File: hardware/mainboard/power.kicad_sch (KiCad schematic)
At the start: 19 parts, among them J1 Eurorack Power, U1 LD1117-3.3, U2 LM4040DBZ-10

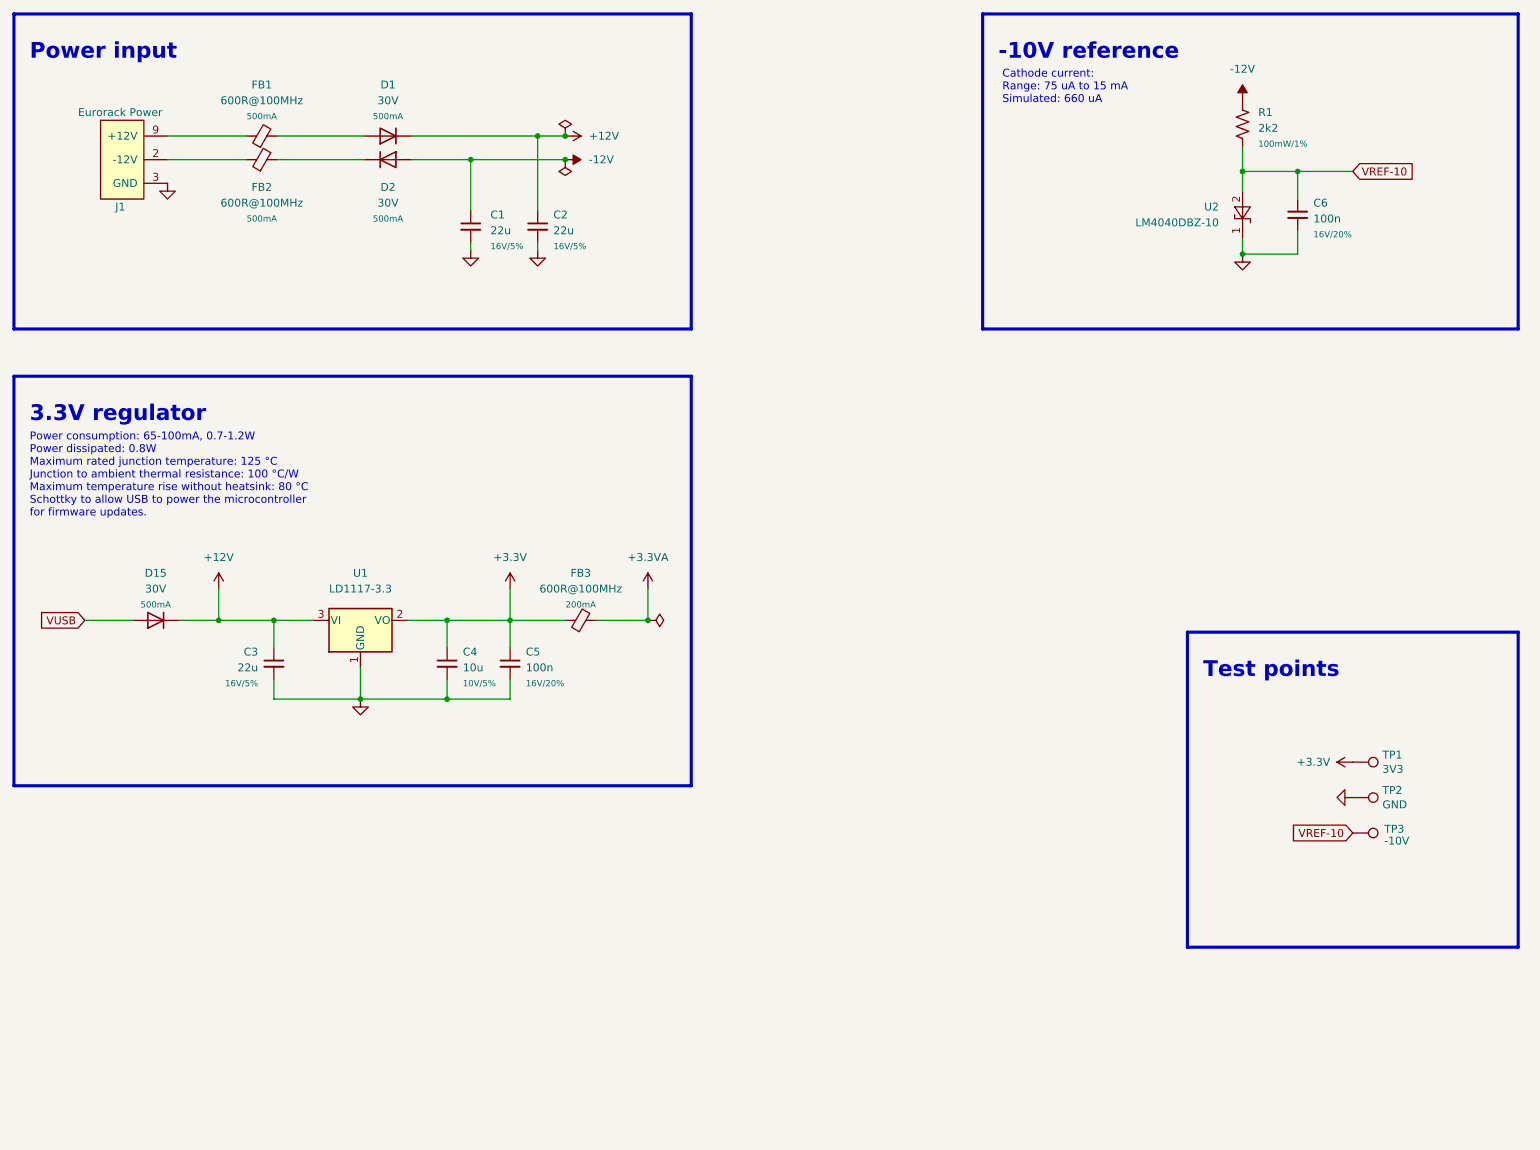
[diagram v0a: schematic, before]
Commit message: hardware: minor tweaks to power schematic's layout
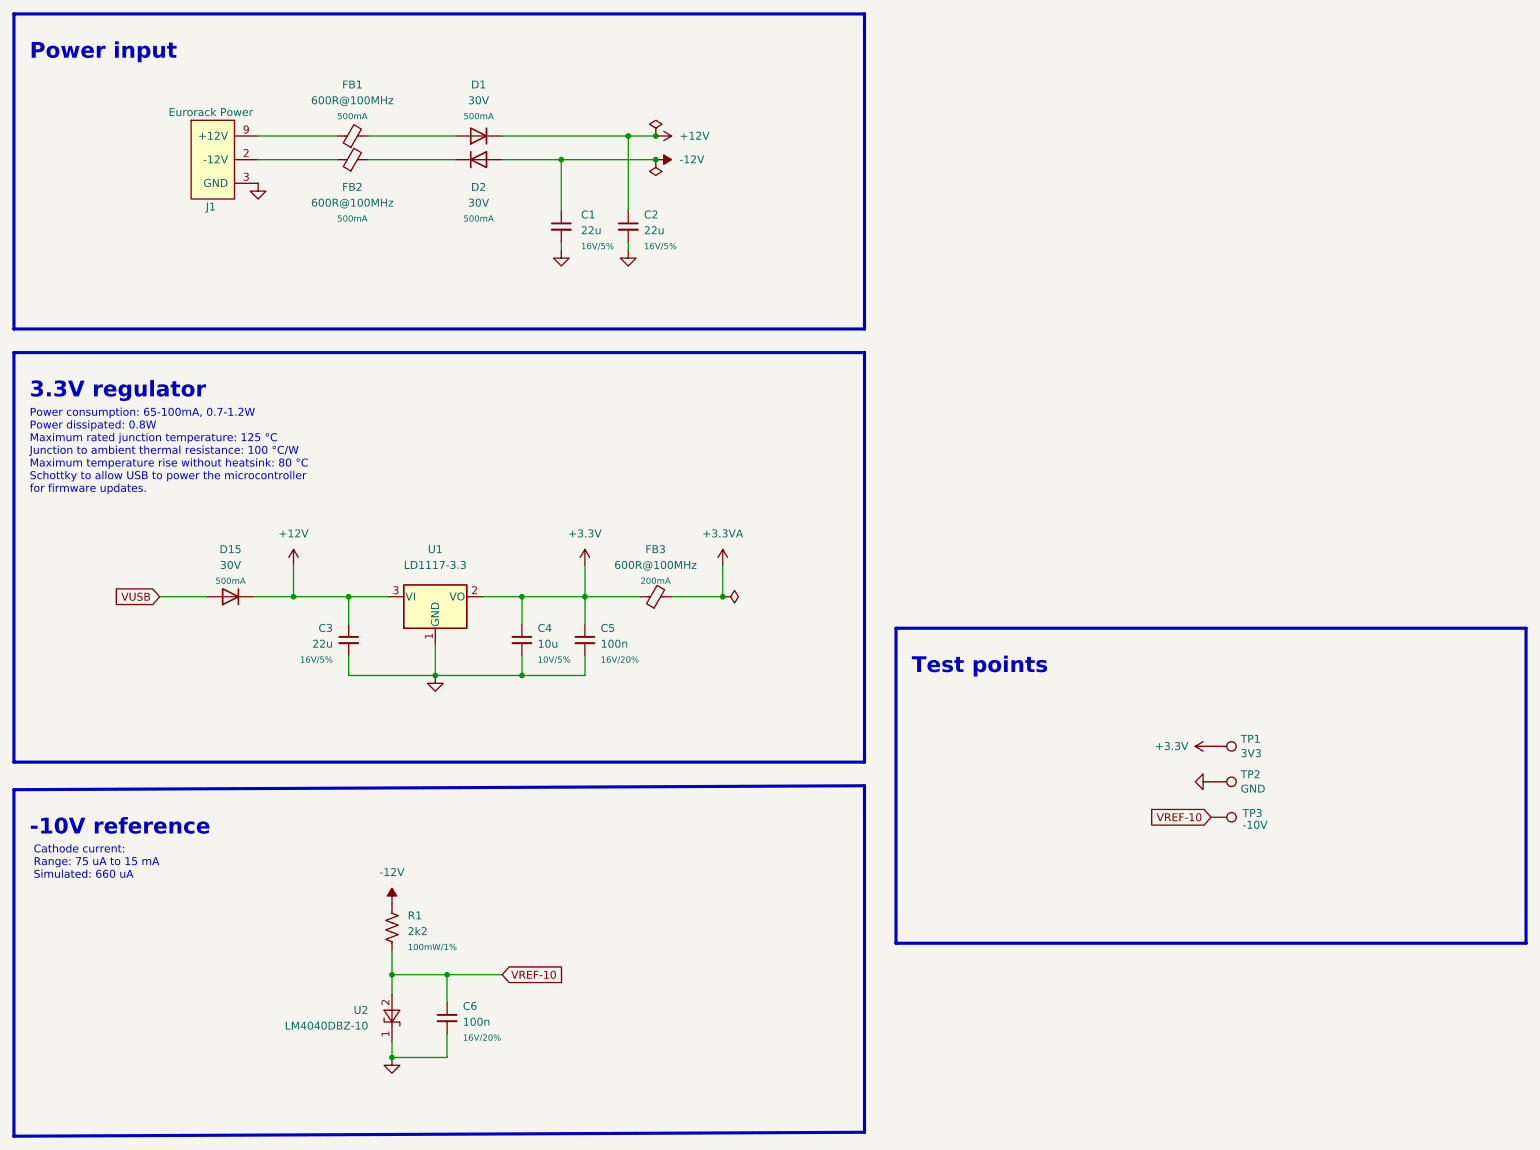
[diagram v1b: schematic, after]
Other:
- moved on the sheet: C1, C2, C3, C4, C5, C6, D1, D15, D2, FB1, FB2, FB3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

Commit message: hardware: use winterbloom footprints for C, R, and L
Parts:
- C1, C2, C3: footprint Capacitor_SMD:C_0805_2012Metric_Pad1.18x1.45mm_HandSolder -> winterbloom:C_0805_HandSolder
- C4: footprint Capacitor_SMD:C_0603_1608Metric_Pad1.08x0.95mm_HandSolder -> winterbloom:C_0603_HandSolder
- C5, C6: footprint Capacitor_SMD:C_0402_1005Metric_Pad0.74x0.62mm_HandSolder -> winterbloom:C_0402_HandSolder
- FB1, FB2, FB3: footprint Inductor_SMD:L_0603_1608Metric_Pad1.05x0.95mm_HandSolder -> winterbloom:L_0603_HandSolder
- R1: footprint Resistor_SMD:R_0402_1005Metric_Pad0.72x0.64mm_HandSolder -> winterbloom:R_0402_HandSolder
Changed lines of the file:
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@@
       (effects (font (size 1.27 1.27)) (justify right))
     )
-    (property "Footprint" "Capacitor_SMD:C_0805_2012Metric_Pad1.18x1.45mm_HandSolder" (id 2) (at 71.755 118.745 0)
+    (property "Footprint" "winterbloom:C_0805_HandSolder" (id 2) (at 71.755 118.745 0)
       (effects (font (size 1.27 1.27)) hide)
     )
@@
       (effects (font (size 1.27 1.27)) (justify left))
     )
-    (property "Footprint" "Capacitor_SMD:C_0603_1608Metric_Pad1.08x0.95mm_HandSolder" (id 2) (at 99.695 118.745 0)
+    (property "Footprint" "winterbloom:C_0603_HandSolder" (id 2) (at 99.695 118.745 0)
       (effects (font (size 1.27 1.27)) hide)
     )
@@
       (effects (font (size 1.27 1.27)) (justify left))
     )
-    (property "Footprint" "Capacitor_SMD:C_0402_1005Metric_Pad0.74x0.62mm_HandSolder" (id 2) (at 110.8202 122.555 0)
+    (property "Footprint" "winterbloom:C_0402_HandSolder" (id 2) (at 110.8202 122.555 0)
       (effects (font (size 1.27 1.27)) hide)
     )
@@
     (property "Reference" "FB3" (id 0) (at 121.2469 104.14 90))
     (property "Value" "600R@100MHz" (id 1) (at 121.2469 106.68 90))
-    (property "Footprint" "Inductor_SMD:L_0603_1608Metric_Pad1.05x0.95mm_HandSolder" (id 2) (at 121.285 113.538 90)
+    (property "Footprint" "winterbloom:L_0603_HandSolder" (id 2) (at 121.285 113.538 90)
       (effects (font (size 1.27 1.27)) hide)
     )
@@
     (property "Reference" "FB2" (id 0) (at 72.3519 45.72 90))
     (property "Value" "600R@100MHz" (id 1) (at 72.3519 48.26 90))
-    (property "Footprint" "Inductor_SMD:L_0603_1608Metric_Pad1.05x0.95mm_HandSolder" (id 2) (at 72.39 43.053 90)
+    (property "Footprint" "winterbloom:L_0603_HandSolder" (id 2) (at 72.39 43.053 90)
       (effects (font (size 1.27 1.27)) hide)
     )
@@
     (property "Reference" "FB1" (id 0) (at 72.3519 29.21 90))
     (property "Value" "600R@100MHz" (id 1) (at 72.3519 31.75 90))
-    (property "Footprint" "Inductor_SMD:L_0603_1608Metric_Pad1.05x0.95mm_HandSolder" (id 2) (at 72.39 39.243 90)
+    (property "Footprint" "winterbloom:L_0603_HandSolder" (id 2) (at 72.39 39.243 90)
       (effects (font (size 1.27 1.27)) hide)
     )
@@
       (effects (font (size 1.27 1.27)) (justify left))
     )
-    (property "Footprint" "Resistor_SMD:R_0402_1005Metric_Pad0.72x0.64mm_HandSolder" (id 2) (at 79.756 165.354 90)
+    (property "Footprint" "winterbloom:R_0402_HandSolder" (id 2) (at 79.756 165.354 90)
       (effects (font (size 1.27 1.27)) hide)
     )
@@
       (effects (font (size 1.27 1.27)) (justify left))
     )
-    (property "Footprint" "Capacitor_SMD:C_0402_1005Metric_Pad0.74x0.62mm_HandSolder" (id 2) (at 88.5952 183.515 0)
+    (property "Footprint" "winterbloom:C_0402_HandSolder" (id 2) (at 88.5952 183.515 0)
       (effects (font (size 1.27 1.27)) hide)
     )
@@
       (effects (font (size 1.27 1.27)) (justify left))
     )
-    (property "Footprint" "Capacitor_SMD:C_0805_2012Metric_Pad1.18x1.45mm_HandSolder" (id 2) (at 107.0102 55.88 0)
+    (property "Footprint" "winterbloom:C_0805_HandSolder" (id 2) (at 107.0102 55.88 0)
       (effects (font (size 1.27 1.27)) hide)
     )
@@
       (effects (font (size 1.27 1.27)) (justify left))
     )
-    (property "Footprint" "Capacitor_SMD:C_0805_2012Metric_Pad1.18x1.45mm_HandSolder" (id 2) (at 117.8052 55.88 0)
-      (effects (font (size 1.27 1.27)) hide)
-    )
+    (property "Footprint" "winterbloom:C_0805_HandSolder" (id 2) (at 117.8052 55.88 0)
+      (effects (font (size 1.27 1.27)) hide)
+    )

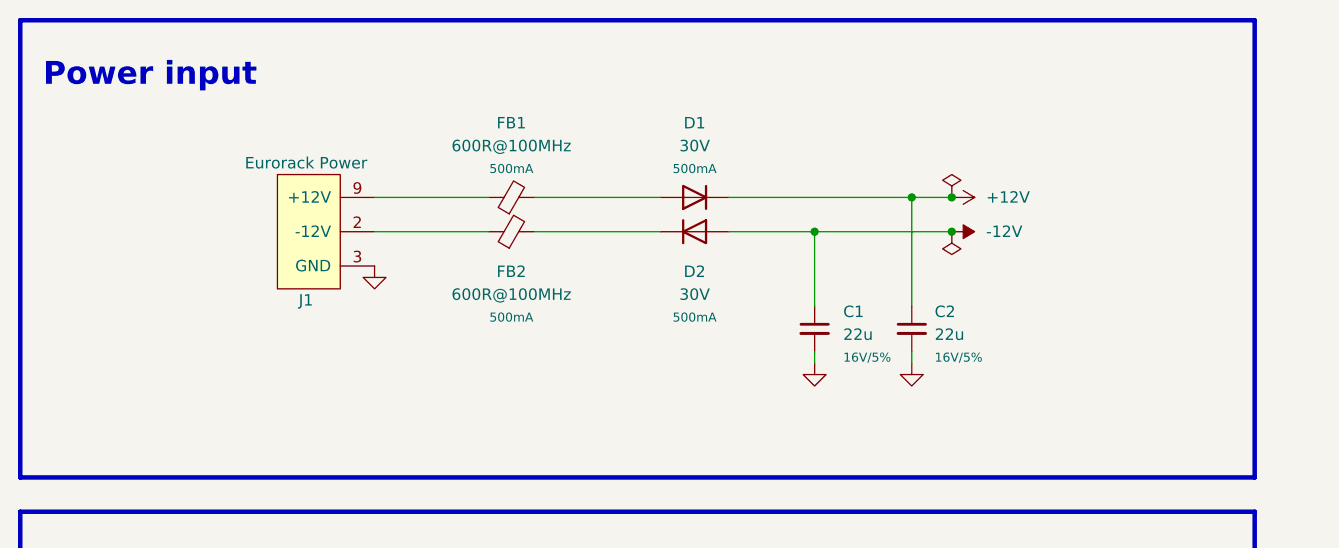
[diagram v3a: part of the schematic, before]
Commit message: hardware: spruce up some labels
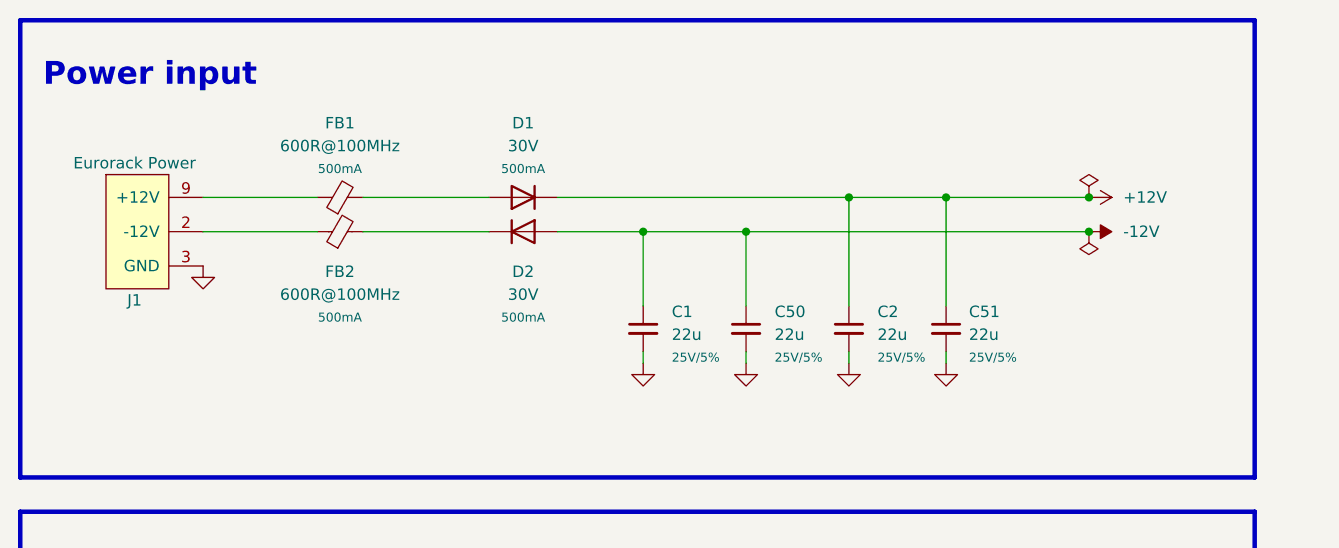
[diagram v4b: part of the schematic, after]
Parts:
- added C50, C51: 22u, winterbloom:C_0805_HandSolder, symbol Device:C_Small
- C1, C2: Rating 16V/5% -> 25V/5%
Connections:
- net +12V: now also C51.1
- net -12V: now also C50.1
- net GND: now also C50.2, C51.2
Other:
- moved on the sheet: C1, C2, D1, D2, FB1, FB2, J1

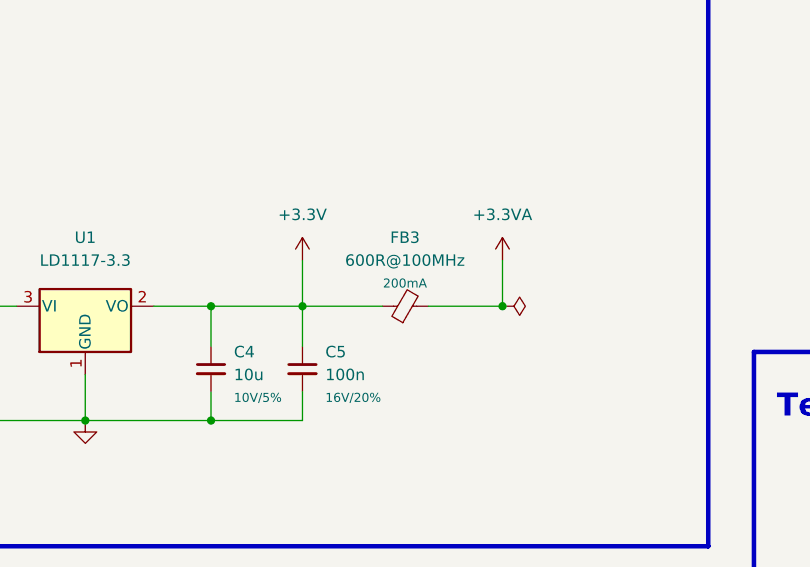
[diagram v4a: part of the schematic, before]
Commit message: hardware: update some labels, fix some fields, re-do fancytext
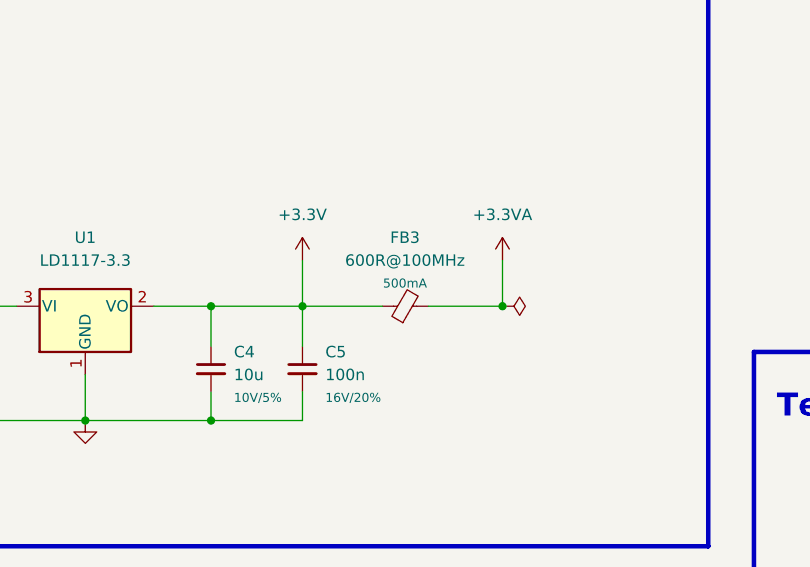
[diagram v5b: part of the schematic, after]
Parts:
- FB3: Rating 200mA -> 500mA
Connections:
- net +3V3 renamed +3.3V
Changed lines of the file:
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@@
       (effects (font (size 1.27 1.27)) hide)
     )
-    (property "Rating" "200mA" (id 8) (at 121.2469 109.22 90)
+    (property "Rating" "500mA" (id 8) (at 121.2469 109.22 90)
       (effects (font (size 1 1)))
     )
